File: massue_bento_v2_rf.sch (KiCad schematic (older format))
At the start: 15 parts, among them P11 TST, P12 TST, P13 TST, P14 TST, P15 TST, U5 CC3000

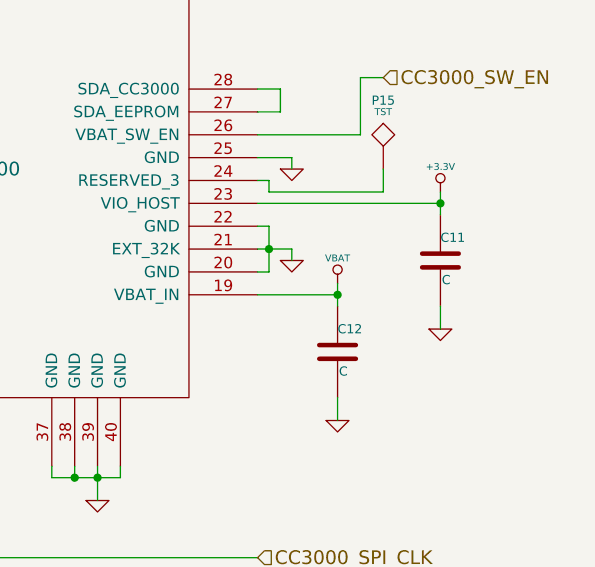
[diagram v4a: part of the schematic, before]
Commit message: New : AT42 sensor
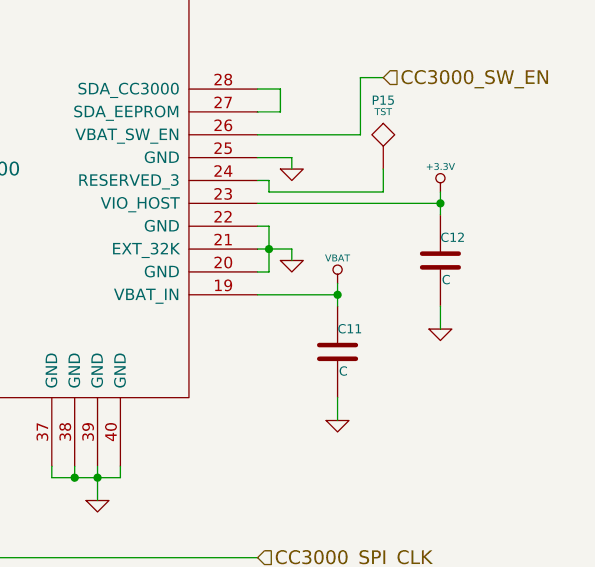
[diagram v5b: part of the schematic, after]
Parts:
- renumbered C12 to C11, C11 to C12
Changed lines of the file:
@@
 EESchema Schematic File Version 2
 LIBS:power
+LIBS:tom_kicad
 LIBS:device
-LIBS:transistors
 LIBS:conn
-LIBS:linear
-LIBS:regul
-LIBS:74xx
-LIBS:cmos4000
-LIBS:adc-dac
-LIBS:memory
-LIBS:xilinx
-LIBS:special
-LIBS:microcontrollers
-LIBS:dsp
-LIBS:microchip
-LIBS:analog_switches
-LIBS:motorola
-LIBS:texas
-LIBS:intel
-LIBS:audio
-LIBS:interface
-LIBS:digital-audio
-LIBS:philips
-LIBS:display
-LIBS:cypress
-LIBS:siliconi
-LIBS:opto
-LIBS:atmel
-LIBS:contrib
-LIBS:valves
-LIBS:tom_kicad
 LIBS:massue_bento_v2-cache
 EELAYER 24 0
@@
 $EndComp
 $Comp
-L GND #PWR040
+L GND #PWR041
 U 1 1 53A57B5B
 P 4400 3450
-F 0 "#PWR040" H 4400 3450 30  0001 C CNN
+F 0 "#PWR041" H 4400 3450 30  0001 C CNN
 F 1 "GND" H 4400 3380 30  0001 C CNN
 F 2 "" H 4400 3450 60  0000 C CNN
@@
 $EndComp
 $Comp
-L GND #PWR041
+L GND #PWR042
 U 1 1 53A57DBF
 P 2350 4700
-F 0 "#PWR041" H 2350 4700 30  0001 C CNN
+F 0 "#PWR042" H 2350 4700 30  0001 C CNN
 F 1 "GND" H 2350 4630 30  0001 C CNN
 F 2 "" H 2350 4700 60  0000 C CNN
@@
 WL_EN2
 $Comp
-L GND #PWR042
+L GND #PWR043
 U 1 1 53A57EDD
 P 4400 4400
-F 0 "#PWR042" H 4400 4400 30  0001 C CNN
+F 0 "#PWR043" H 4400 4400 30  0001 C CNN
 F 1 "GND" H 4400 4330 30  0001 C CNN
 F 2 "" H 4400 4400 60  0000 C CNN
@@
 Connection ~ 4400 4300
 $Comp
-L GND #PWR043
+L GND #PWR044
 U 1 1 53A57FA7
 P 5050 5200
-F 0 "#PWR043" H 5050 5200 30  0001 C CNN
+F 0 "#PWR044" H 5050 5200 30  0001 C CNN
 F 1 "GND" H 5050 5130 30  0001 C CNN
 F 2 "" H 5050 5200 60  0000 C CNN
@@
 $EndComp
 $Comp
-L GND #PWR044
+L GND #PWR045
 U 1 1 53A57FB9
 P 5750 5200
-F 0 "#PWR044" H 5750 5200 30  0001 C CNN
+F 0 "#PWR045" H 5750 5200 30  0001 C CNN
 F 1 "GND" H 5750 5130 30  0001 C CNN
 F 2 "" H 5750 5200 60  0000 C CNN
@@
 $EndComp
 $Comp
-L GND #PWR045
+L GND #PWR046
 U 1 1 53A57FCB
 P 6300 5200
-F 0 "#PWR045" H 6300 5200 30  0001 C CNN
+F 0 "#PWR046" H 6300 5200 30  0001 C CNN
 F 1 "GND" H 6300 5130 30  0001 C CNN
 F 2 "" H 6300 5200 60  0000 C CNN
@@
 	5550 5050 5550 5200
 $Comp
-L GND #PWR046
+L GND #PWR047
 U 1 1 53A58109
 P 5550 5200
-F 0 "#PWR046" H 5550 5200 30  0001 C CNN
+F 0 "#PWR047" H 5550 5200 30  0001 C CNN
 F 1 "GND" H 5550 5130 30  0001 C CNN
 F 2 "" H 5550 5200 60  0000 C CNN
@@
 CC3000_SPI_CS
 $Comp
-L GND #PWR047
+L GND #PWR048
 U 1 1 53A5852D
 P 7150 4150
-F 0 "#PWR047" H 7150 4150 30  0001 C CNN
+F 0 "#PWR048" H 7150 4150 30  0001 C CNN
 F 1 "GND" H 7150 4080 30  0001 C CNN
 F 2 "" H 7150 4150 60  0000 C CNN
@@
 	7150 4100 7150 4150
 $Comp
-L C C12
+L C C11
 U 1 1 53A587B8
 P 7350 4550
-F 0 "C12" H 7350 4650 40  0000 L CNN
+F 0 "C11" H 7350 4650 40  0000 L CNN
 F 1 "C" H 7356 4465 40  0000 L CNN
 F 2 "" H 7388 4400 30  0000 C CNN
@@
 $EndComp
 $Comp
-L GND #PWR048
+L GND #PWR049
 U 1 1 53A58837
 P 7350 4850
-F 0 "#PWR048" H 7350 4850 30  0001 C CNN
+F 0 "#PWR049" H 7350 4850 30  0001 C CNN
 F 1 "GND" H 7350 4780 30  0001 C CNN
 F 2 "" H 7350 4850 60  0000 C CNN
@@
 Connection ~ 7350 4300
 $Comp
-L C C11
+L C C12
 U 1 1 53A58B62
 P 7800 4150
-F 0 "C11" H 7800 4250 40  0000 L CNN
+F 0 "C12" H 7800 4250 40  0000 L CNN
 F 1 "C" H 7806 4065 40  0000 L CNN
 F 2 "" H 7838 4000 30  0000 C CNN
@@
 $EndComp
 $Comp
-L GND #PWR049
+L GND #PWR050
 U 1 1 53A58B68
 P 7800 4450
-F 0 "#PWR049" H 7800 4450 30  0001 C CNN
+F 0 "#PWR050" H 7800 4450 30  0001 C CNN
 F 1 "GND" H 7800 4380 30  0001 C CNN
 F 2 "" H 7800 4450 60  0000 C CNN
@@
 	7800 3850 7800 3950
 $Comp
-L +3.3V #PWR050
+L +3.3V #PWR051
 U 1 1 53A58B71
 P 7800 3850
-F 0 "#PWR050" H 7800 3810 30  0001 C CNN
+F 0 "#PWR051" H 7800 3810 30  0001 C CNN
 F 1 "+3.3V" H 7800 3960 30  0000 C CNN
 F 2 "" H 7800 3850 60  0000 C CNN
@@
 	7550 3750 7550 3850
 $Comp
-L GND #PWR051
+L GND #PWR052
 U 1 1 53A58F4A
 P 7150 3750
-F 0 "#PWR051" H 7150 3750 30  0001 C CNN
+F 0 "#PWR052" H 7150 3750 30  0001 C CNN
 F 1 "GND" H 7150 3680 30  0001 C CNN
 F 2 "" H 7150 3750 60  0000 C CNN
@@
 	5750 2300 5750 2400
 $Comp
-L GND #PWR052
+L GND #PWR053
 U 1 1 53A5961E
 P 6550 2500
-F 0 "#PWR052" H 6550 2500 30  0001 C CNN
+F 0 "#PWR053" H 6550 2500 30  0001 C CNN
 F 1 "GND" H 6550 2430 30  0001 C CNN
 F 2 "" H 6550 2500 60  0000 C CNN
@@
 Connection ~ 6400 2300
 $Comp
-L GND #PWR053
+L GND #PWR054
 U 1 1 53A59CEE
 P 4900 2500
-F 0 "#PWR053" H 4900 2500 30  0001 C CNN
+F 0 "#PWR054" H 4900 2500 30  0001 C CNN
 F 1 "GND" H 4900 2430 30  0001 C CNN
 F 2 "" H 4900 2500 60  0000 C CNN
@@
 $EndComp
 $Comp
-L GND #PWR054
+L GND #PWR055
 U 1 1 53A5A40B
 P 3950 2400
-F 0 "#PWR054" H 3950 2400 30  0001 C CNN
+F 0 "#PWR055" H 3950 2400 30  0001 C CNN
 F 1 "GND" H 3950 2330 30  0001 C CNN
 F 2 "" H 3950 2400 60  0000 C CNN
@@
 $EndComp
 $Comp
-L GND #PWR055
+L GND #PWR056
 U 1 1 53A5A45C
 P 3050 2400
-F 0 "#PWR055" H 3050 2400 30  0001 C CNN
+F 0 "#PWR056" H 3050 2400 30  0001 C CNN
 F 1 "GND" H 3050 2330 30  0001 C CNN
 F 2 "" H 3050 2400 60  0000 C CNN
@@
 	2550 1600 2550 1450
 $Comp
-L VBAT #PWR056
+L VBAT #PWR057
 U 1 1 53A58531
 P 7350 4250
-F 0 "#PWR056" H 7350 4310 30  0001 C CNN
+F 0 "#PWR057" H 7350 4310 30  0001 C CNN
 F 1 "VBAT" H 7350 4360 30  0000 C CNN
 F 2 "" H 7350 4250 60  0000 C CNN

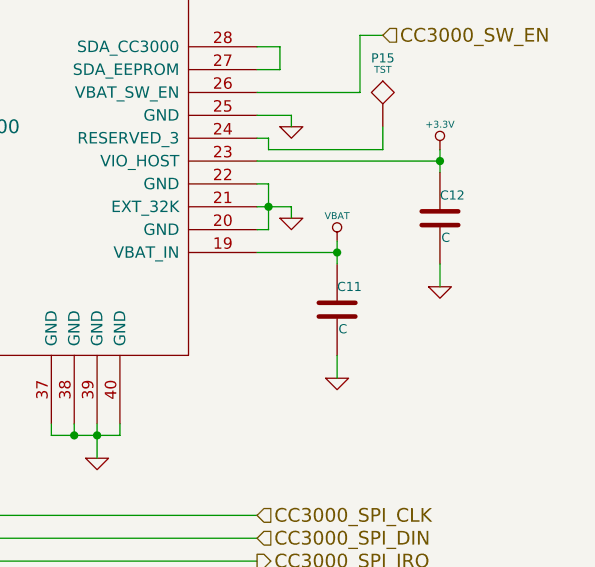
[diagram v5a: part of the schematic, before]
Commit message: New: association of footprints and components
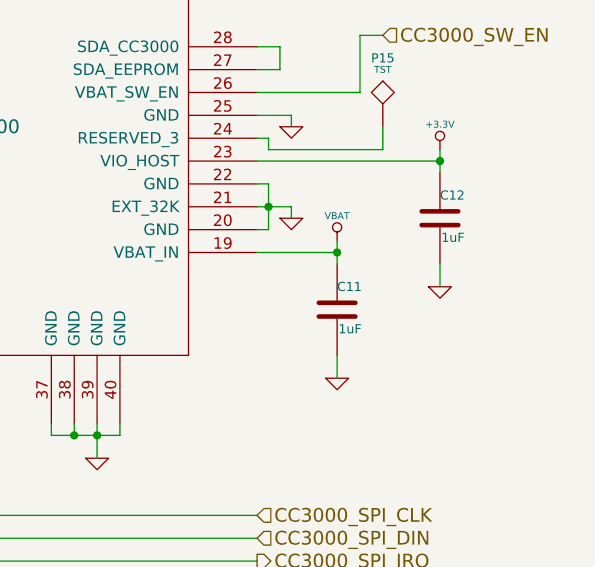
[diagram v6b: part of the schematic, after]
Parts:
- C11, C12: value C -> 1uF
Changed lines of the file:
@@
 EESchema Schematic File Version 2
 LIBS:power
+LIBS:device
+LIBS:transistors
+LIBS:conn
+LIBS:linear
+LIBS:regul
+LIBS:74xx
+LIBS:cmos4000
+LIBS:adc-dac
+LIBS:memory
+LIBS:xilinx
+LIBS:special
+LIBS:microcontrollers
+LIBS:dsp
+LIBS:microchip
+LIBS:analog_switches
+LIBS:motorola
+LIBS:texas
+LIBS:intel
+LIBS:audio
+LIBS:interface
+LIBS:digital-audio
+LIBS:philips
+LIBS:display
+LIBS:cypress
+LIBS:siliconi
+LIBS:opto
+LIBS:atmel
+LIBS:contrib
+LIBS:valves
 LIBS:tom_kicad
-LIBS:device
-LIBS:conn
 LIBS:massue_bento_v2-cache
 EELAYER 24 0
@@
 $EndComp
 $Comp
-L GND #PWR041
+L GND #PWR040
 U 1 1 53A57B5B
 P 4400 3450
-F 0 "#PWR041" H 4400 3450 30  0001 C CNN
+F 0 "#PWR040" H 4400 3450 30  0001 C CNN
 F 1 "GND" H 4400 3380 30  0001 C CNN
 F 2 "" H 4400 3450 60  0000 C CNN
@@
 $EndComp
 $Comp
-L GND #PWR042
+L GND #PWR041
 U 1 1 53A57DBF
 P 2350 4700
-F 0 "#PWR042" H 2350 4700 30  0001 C CNN
+F 0 "#PWR041" H 2350 4700 30  0001 C CNN
 F 1 "GND" H 2350 4630 30  0001 C CNN
 F 2 "" H 2350 4700 60  0000 C CNN
@@
 WL_EN2
 $Comp
-L GND #PWR043
+L GND #PWR042
 U 1 1 53A57EDD
 P 4400 4400
-F 0 "#PWR043" H 4400 4400 30  0001 C CNN
+F 0 "#PWR042" H 4400 4400 30  0001 C CNN
 F 1 "GND" H 4400 4330 30  0001 C CNN
 F 2 "" H 4400 4400 60  0000 C CNN
@@
 Connection ~ 4400 4300
 $Comp
-L GND #PWR044
+L GND #PWR043
 U 1 1 53A57FA7
 P 5050 5200
-F 0 "#PWR044" H 5050 5200 30  0001 C CNN
+F 0 "#PWR043" H 5050 5200 30  0001 C CNN
 F 1 "GND" H 5050 5130 30  0001 C CNN
 F 2 "" H 5050 5200 60  0000 C CNN
@@
 $EndComp
 $Comp
-L GND #PWR045
+L GND #PWR044
 U 1 1 53A57FB9
 P 5750 5200
-F 0 "#PWR045" H 5750 5200 30  0001 C CNN
+F 0 "#PWR044" H 5750 5200 30  0001 C CNN
 F 1 "GND" H 5750 5130 30  0001 C CNN
 F 2 "" H 5750 5200 60  0000 C CNN
@@
 $EndComp
 $Comp
-L GND #PWR046
+L GND #PWR045
 U 1 1 53A57FCB
 P 6300 5200
-F 0 "#PWR046" H 6300 5200 30  0001 C CNN
+F 0 "#PWR045" H 6300 5200 30  0001 C CNN
 F 1 "GND" H 6300 5130 30  0001 C CNN
 F 2 "" H 6300 5200 60  0000 C CNN
@@
 	5550 5050 5550 5200
 $Comp
-L GND #PWR047
+L GND #PWR046
 U 1 1 53A58109
 P 5550 5200
-F 0 "#PWR047" H 5550 5200 30  0001 C CNN
+F 0 "#PWR046" H 5550 5200 30  0001 C CNN
 F 1 "GND" H 5550 5130 30  0001 C CNN
 F 2 "" H 5550 5200 60  0000 C CNN
@@
 CC3000_SPI_CS
 $Comp
-L GND #PWR048
+L GND #PWR047
 U 1 1 53A5852D
 P 7150 4150
-F 0 "#PWR048" H 7150 4150 30  0001 C CNN
+F 0 "#PWR047" H 7150 4150 30  0001 C CNN
 F 1 "GND" H 7150 4080 30  0001 C CNN
 F 2 "" H 7150 4150 60  0000 C CNN
@@
 P 7350 4550
 F 0 "C11" H 7350 4650 40  0000 L CNN
-F 1 "C" H 7356 4465 40  0000 L CNN
+F 1 "1uF" H 7356 4465 40  0000 L CNN
 F 2 "" H 7388 4400 30  0000 C CNN
 F 3 "" H 7350 4550 60  0000 C CNN
@@
 $EndComp
 $Comp
-L GND #PWR049
+L GND #PWR048
 U 1 1 53A58837
 P 7350 4850
-F 0 "#PWR049" H 7350 4850 30  0001 C CNN
+F 0 "#PWR048" H 7350 4850 30  0001 C CNN
 F 1 "GND" H 7350 4780 30  0001 C CNN
 F 2 "" H 7350 4850 60  0000 C CNN
@@
 P 7800 4150
 F 0 "C12" H 7800 4250 40  0000 L CNN
-F 1 "C" H 7806 4065 40  0000 L CNN
+F 1 "1uF" H 7806 4065 40  0000 L CNN
 F 2 "" H 7838 4000 30  0000 C CNN
 F 3 "" H 7800 4150 60  0000 C CNN
@@
 $EndComp
 $Comp
-L GND #PWR050
+L GND #PWR049
 U 1 1 53A58B68
 P 7800 4450
-F 0 "#PWR050" H 7800 4450 30  0001 C CNN
+F 0 "#PWR049" H 7800 4450 30  0001 C CNN
 F 1 "GND" H 7800 4380 30  0001 C CNN
 F 2 "" H 7800 4450 60  0000 C CNN
@@
 	7800 3850 7800 3950
 $Comp
-L +3.3V #PWR051
+L +3.3V #PWR050
 U 1 1 53A58B71
 P 7800 3850
-F 0 "#PWR051" H 7800 3810 30  0001 C CNN
+F 0 "#PWR050" H 7800 3810 30  0001 C CNN
 F 1 "+3.3V" H 7800 3960 30  0000 C CNN
 F 2 "" H 7800 3850 60  0000 C CNN
@@
 	7550 3750 7550 3850
 $Comp
-L GND #PWR052
+L GND #PWR051
 U 1 1 53A58F4A
 P 7150 3750
-F 0 "#PWR052" H 7150 3750 30  0001 C CNN
+F 0 "#PWR051" H 7150 3750 30  0001 C CNN
 F 1 "GND" H 7150 3680 30  0001 C CNN
 F 2 "" H 7150 3750 60  0000 C CNN
@@
 	5750 2300 5750 2400
 $Comp
-L GND #PWR053
+L GND #PWR052
 U 1 1 53A5961E
 P 6550 2500
-F 0 "#PWR053" H 6550 2500 30  0001 C CNN
+F 0 "#PWR052" H 6550 2500 30  0001 C CNN
 F 1 "GND" H 6550 2430 30  0001 C CNN
 F 2 "" H 6550 2500 60  0000 C CNN
@@
 Connection ~ 6400 2300
 $Comp
-L GND #PWR054
+L GND #PWR053
 U 1 1 53A59CEE
 P 4900 2500
-F 0 "#PWR054" H 4900 2500 30  0001 C CNN
+F 0 "#PWR053" H 4900 2500 30  0001 C CNN
 F 1 "GND" H 4900 2430 30  0001 C CNN
 F 2 "" H 4900 2500 60  0000 C CNN
@@
 $EndComp
 $Comp
-L GND #PWR055
+L GND #PWR054
 U 1 1 53A5A40B
 P 3950 2400
-F 0 "#PWR055" H 3950 2400 30  0001 C CNN
+F 0 "#PWR054" H 3950 2400 30  0001 C CNN
 F 1 "GND" H 3950 2330 30  0001 C CNN
 F 2 "" H 3950 2400 60  0000 C CNN
@@
 $EndComp
 $Comp
-L GND #PWR056
+L GND #PWR055
 U 1 1 53A5A45C
 P 3050 2400
-F 0 "#PWR056" H 3050 2400 30  0001 C CNN
+F 0 "#PWR055" H 3050 2400 30  0001 C CNN
 F 1 "GND" H 3050 2330 30  0001 C CNN
 F 2 "" H 3050 2400 60  0000 C CNN
@@
 	2550 1600 2550 1450
 $Comp
-L VBAT #PWR057
+L VBAT #PWR056
 U 1 1 53A58531
 P 7350 4250
-F 0 "#PWR057" H 7350 4310 30  0001 C CNN
+F 0 "#PWR056" H 7350 4310 30  0001 C CNN
 F 1 "VBAT" H 7350 4360 30  0000 C CNN
 F 2 "" H 7350 4250 60  0000 C CNN
